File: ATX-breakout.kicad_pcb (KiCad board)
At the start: 2 copper layers, 67 x 59.5 mm, 21 parts, among them J1 I2C, J10 3V3 out, J11 12V out, J2 EPS, J3 USB_A, J4 Raspberry_Pi_2_3, J5 ATX24pin, J6 12V out, J7 pson ext, J8 5V out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

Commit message: Added readme
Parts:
- added G***: LOGO, graphics:kiwi, B.Cu at (114.6, 61.4)
- added G***: LOGO, graphics:kiwi, F.Cu at (69.0, 87.2)
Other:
- board text added: "PowerSelect"
- board text added: "git.io/PiATX"
- board text removed: "USB PowerSelect"

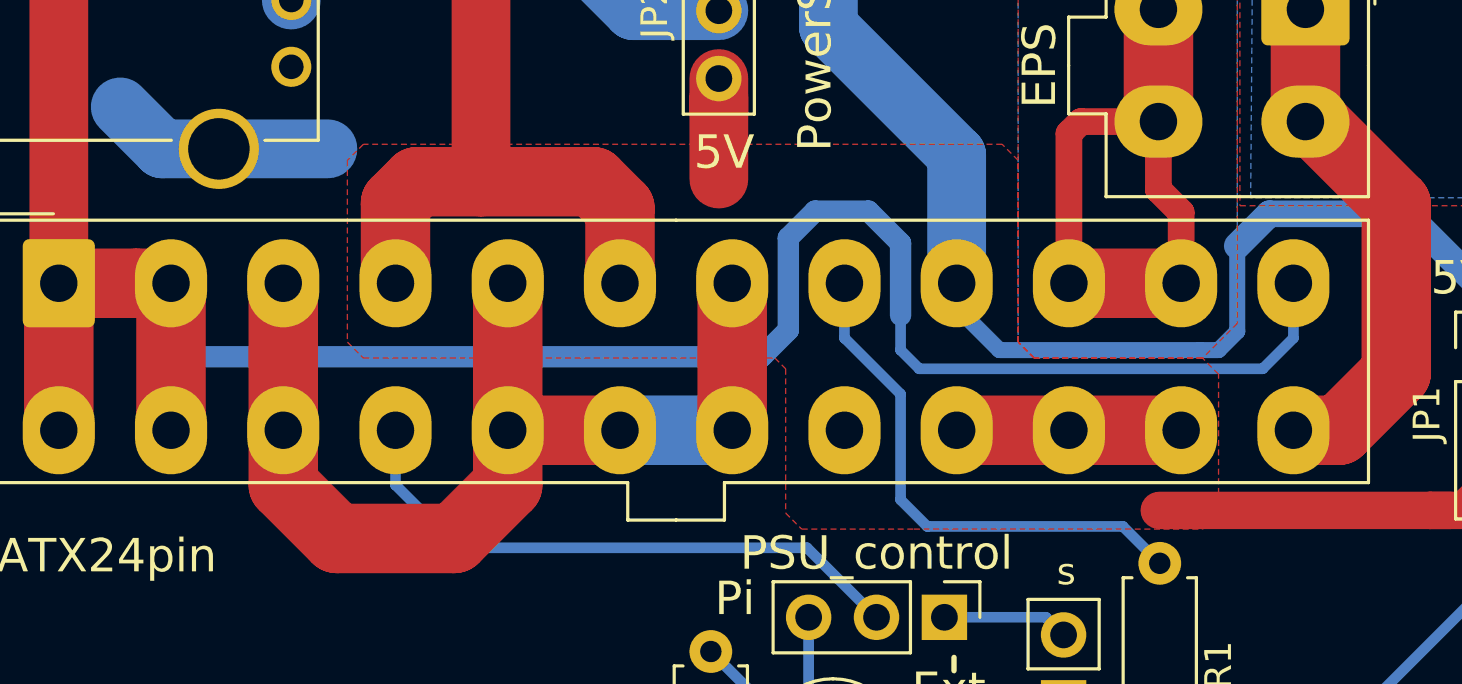
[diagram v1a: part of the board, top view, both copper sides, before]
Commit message: Made 12v pour solid, and increased 5v trace thicknesses
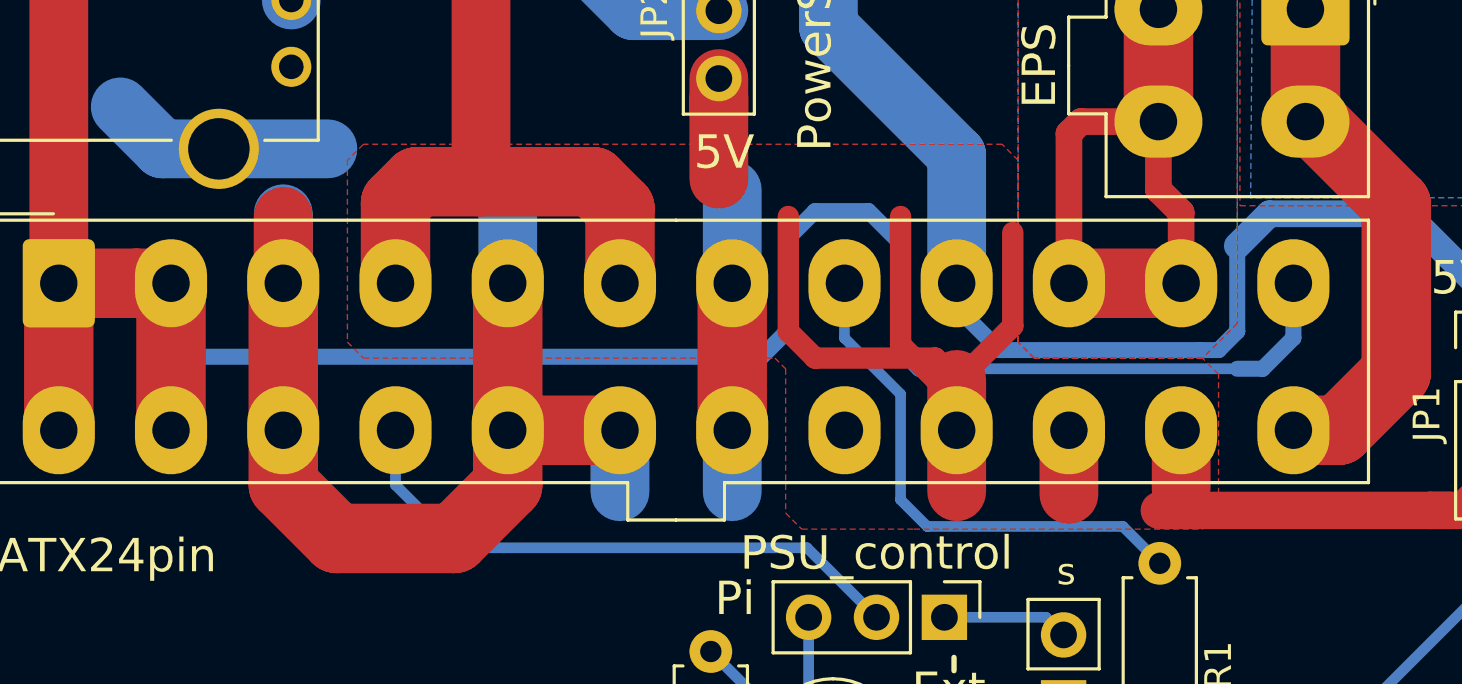
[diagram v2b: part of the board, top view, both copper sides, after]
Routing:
- net +5V: track 61.0 -> 86.6 mm
- net GND: track 107.2 -> 121.7 mm
- net +3V3: track 95.8 -> 96.6 mm

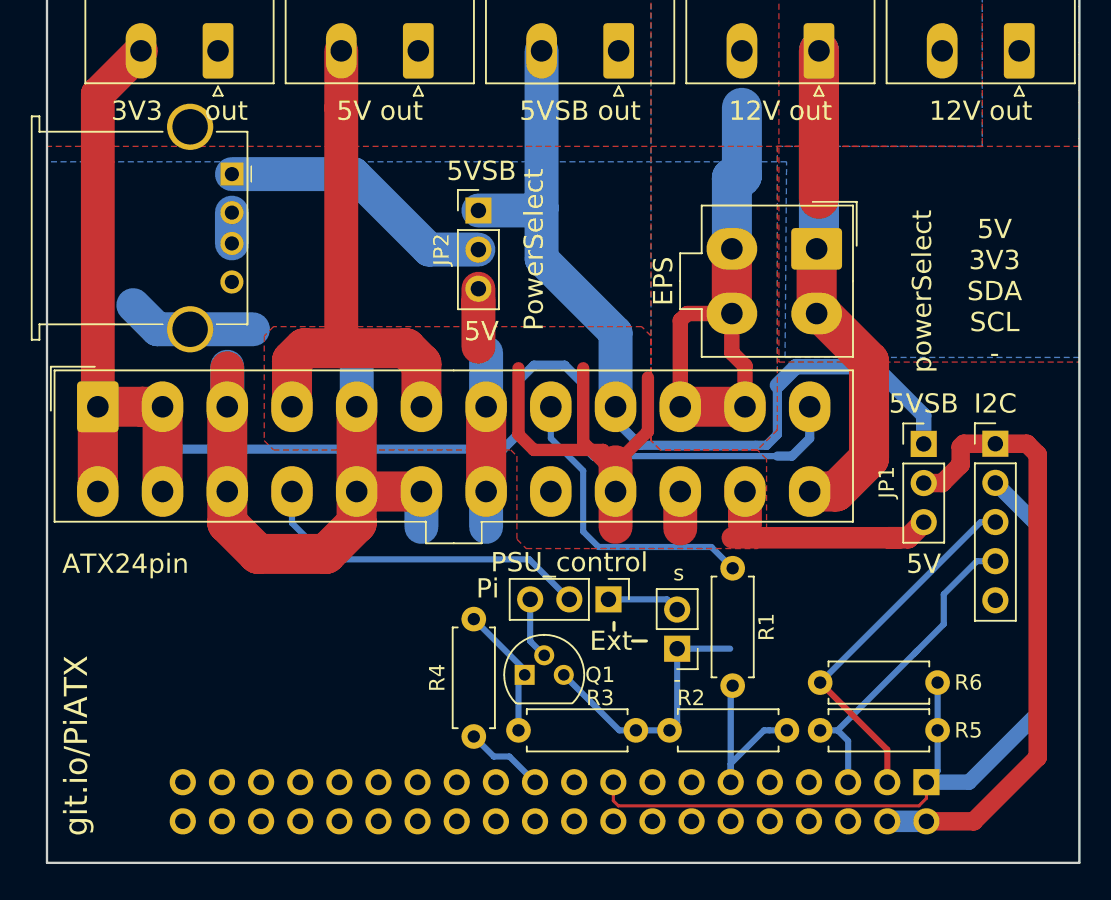
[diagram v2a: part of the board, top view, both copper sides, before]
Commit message: Fixed 3.3v shorted across lots of pins
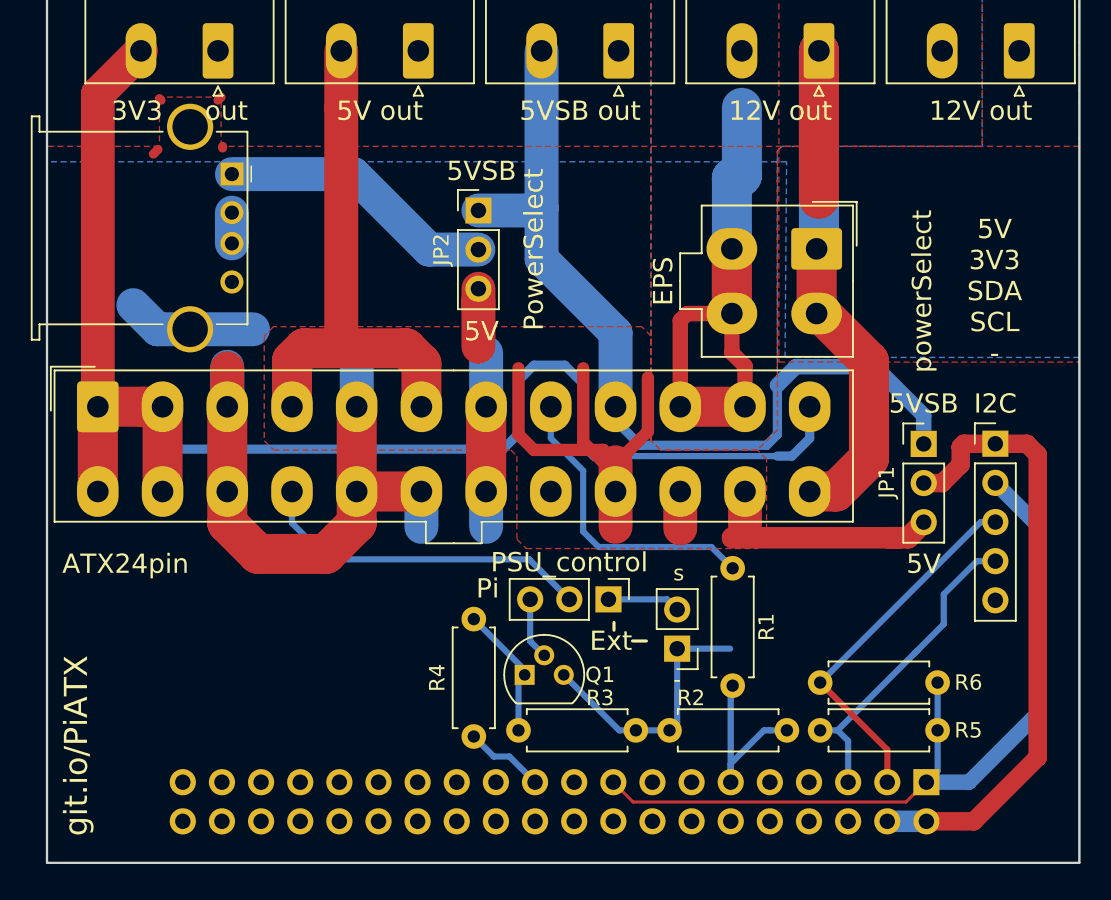
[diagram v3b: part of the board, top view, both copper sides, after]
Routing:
- net /3v3_rpi: track 54.8 -> 53.3 mm
- net (no net): track 0.00 -> 0.95 mm

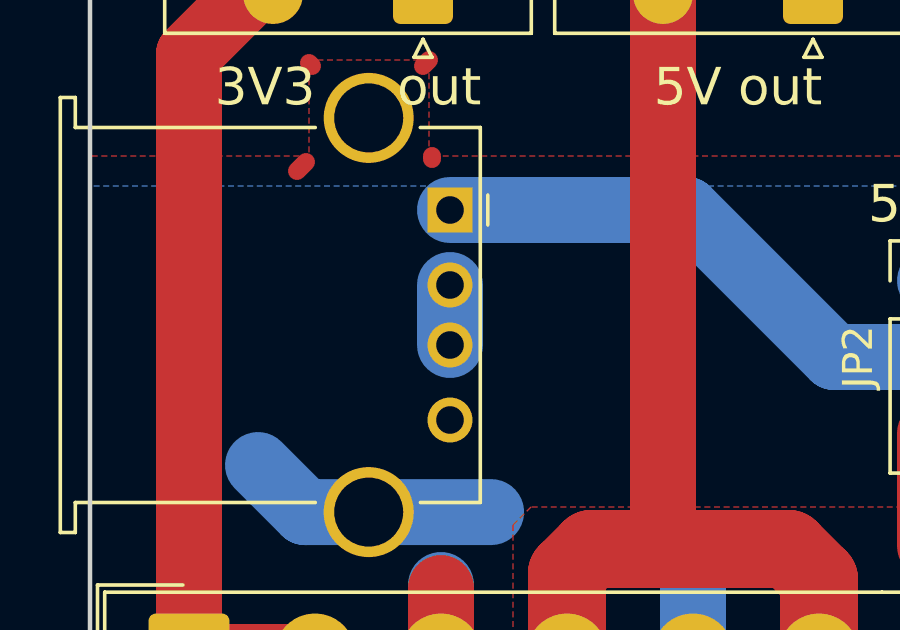
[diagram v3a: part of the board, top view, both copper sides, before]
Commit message: fixed ground-pour weirdness
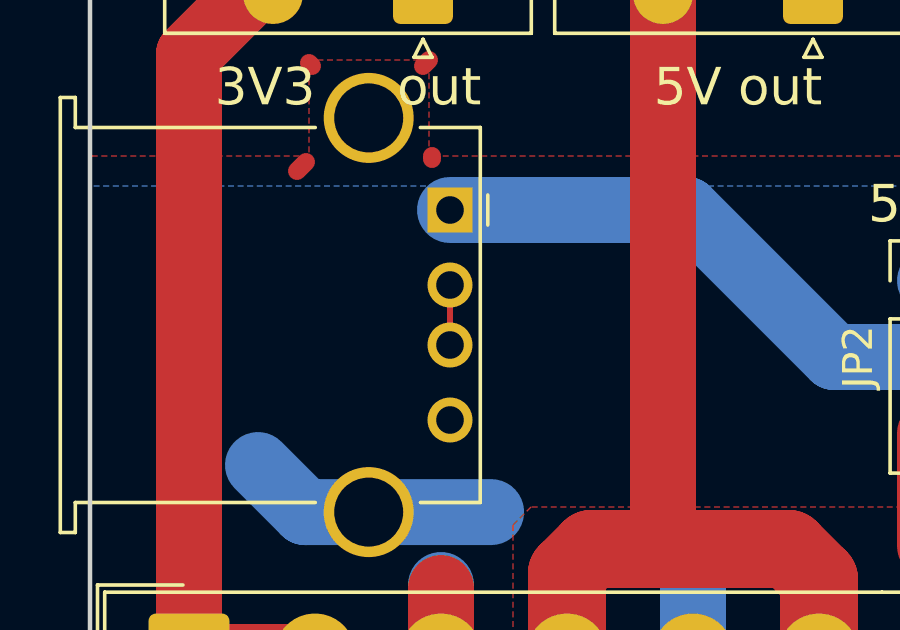
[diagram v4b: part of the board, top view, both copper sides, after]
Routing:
- net (no net): track 0.95 -> 0.00 mm
- net GND: track 121.7 -> 122.7 mm
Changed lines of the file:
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@@
   (gr_line (start 122 100) (end 122 40.5) (layer Edge.Cuts) (width 0.15))
   (gr_line (start 55 100) (end 122 100) (layer Edge.Cuts) (width 0.15))
-  (segment (start 62.4 50.5) (end 62.3 50.4) (width 0.6) (layer F.Cu) (net 0))
-  (segment (start 66.1 50.5) (end 66.3 50.3) (width 0.6) (layer F.Cu) (net 0))
-  (segment (start 66.4 53.5) (end 66.4 53.6) (width 0.6) (layer F.Cu) (net 0))
-  (segment (start 61.9 54) (end 62.2 53.7) (width 0.6) (layer F.Cu) (net 0))
+  (segment (start 62.4 50.5) (end 62.3 50.4) (width 0.6) (layer F.Cu) (net 3))
+  (segment (start 66.1 50.5) (end 66.3 50.3) (width 0.6) (layer F.Cu) (net 3))
+  (segment (start 66.4 53.5) (end 66.4 53.6) (width 0.6) (layer F.Cu) (net 3))
+  (segment (start 61.9 54) (end 62.2 53.7) (width 0.6) (layer F.Cu) (net 3))
   (segment (start 109.534999 97.305001) (end 112.074999 97.305001) (width 1.4) (layer B.Cu) (net 1))
   (segment (start 118.6 72.8) (end 116.55 72.8) (width 1.2) (layer F.Cu) (net 1))
@@
   (segment (start 74.9 55.3) (end 67 55.3) (width 2.2) (layer B.Cu) (net 15))
   (segment (start 79.8 60.2) (end 74.9 55.3) (width 2.2) (layer B.Cu) (net 15))
-  (segment (start 67 59.8) (end 67 57.8) (width 2.2) (layer B.Cu) (net 16))
+  (segment (start 67 57.8) (end 67 59.8) (width 0.2) (layer F.Cu) (net 16))
   (segment (start 109.534999 92.654999) (end 105.18 88.3) (width 0.4) (layer F.Cu) (net 17))
   (segment (start 109.534999 94.765001) (end 109.534999 92.654999) (width 0.4) (layer F.Cu) (net 17))

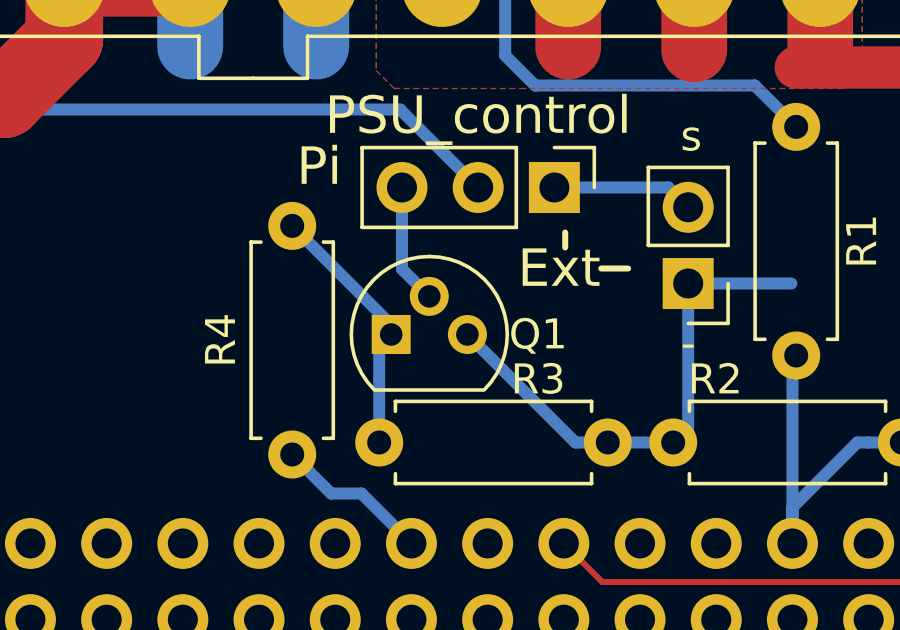
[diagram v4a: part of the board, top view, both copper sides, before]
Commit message: Switched to a more common transistor pinout
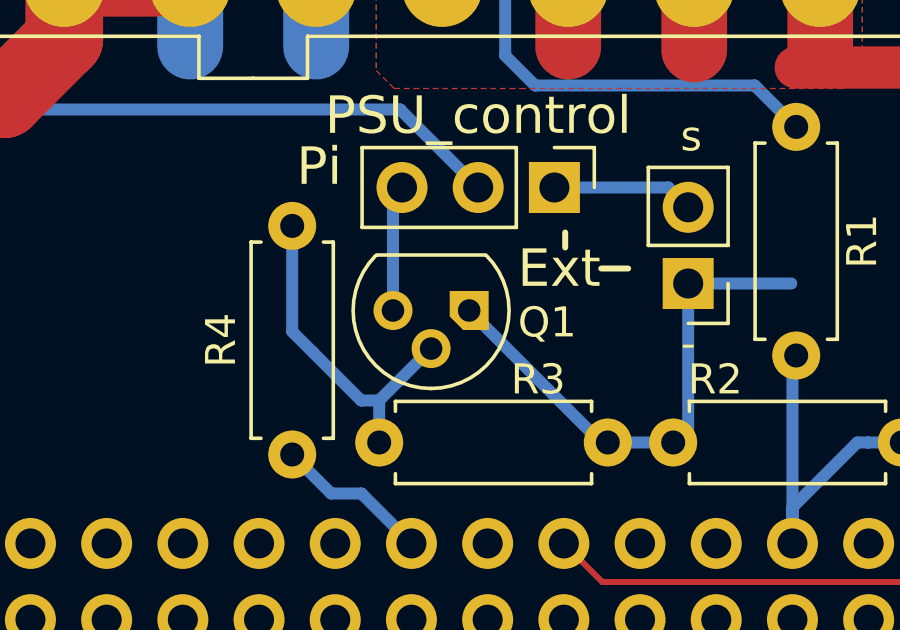
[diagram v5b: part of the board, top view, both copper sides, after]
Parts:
- moved Q1 2.72 mm to (88.6, 87.0), turned to 180 degrees
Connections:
- Q1 pad 1: Net-(Q1-Pad1) -> GND
- Q1 pad 2: Net-(JP3-Pad3) -> Net-(Q1-Pad2)
- Q1 pad 3: GND -> Net-(JP3-Pad3)
- R3 pad 1: Net-(Q1-Pad1) -> Net-(Q1-Pad2)
- R4 pad 2: Net-(Q1-Pad1) -> Net-(Q1-Pad2)
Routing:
- net Net-(Q1-Pad2): track 0.00 -> 11.2 mm
- net Net-(Q1-Pad1): track 8.75 -> 0.00 mm

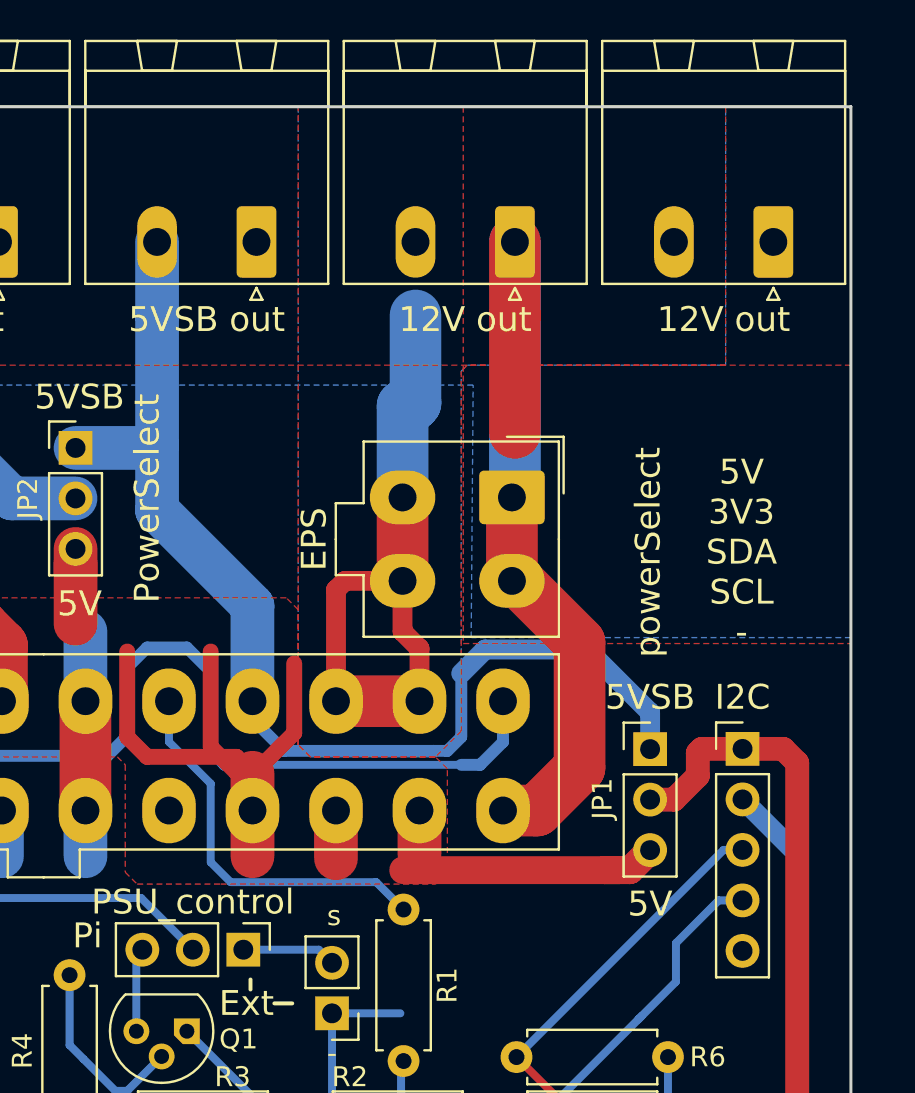
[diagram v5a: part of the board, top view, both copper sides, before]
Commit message: Added third 12v connector, fixed 12v-5v short
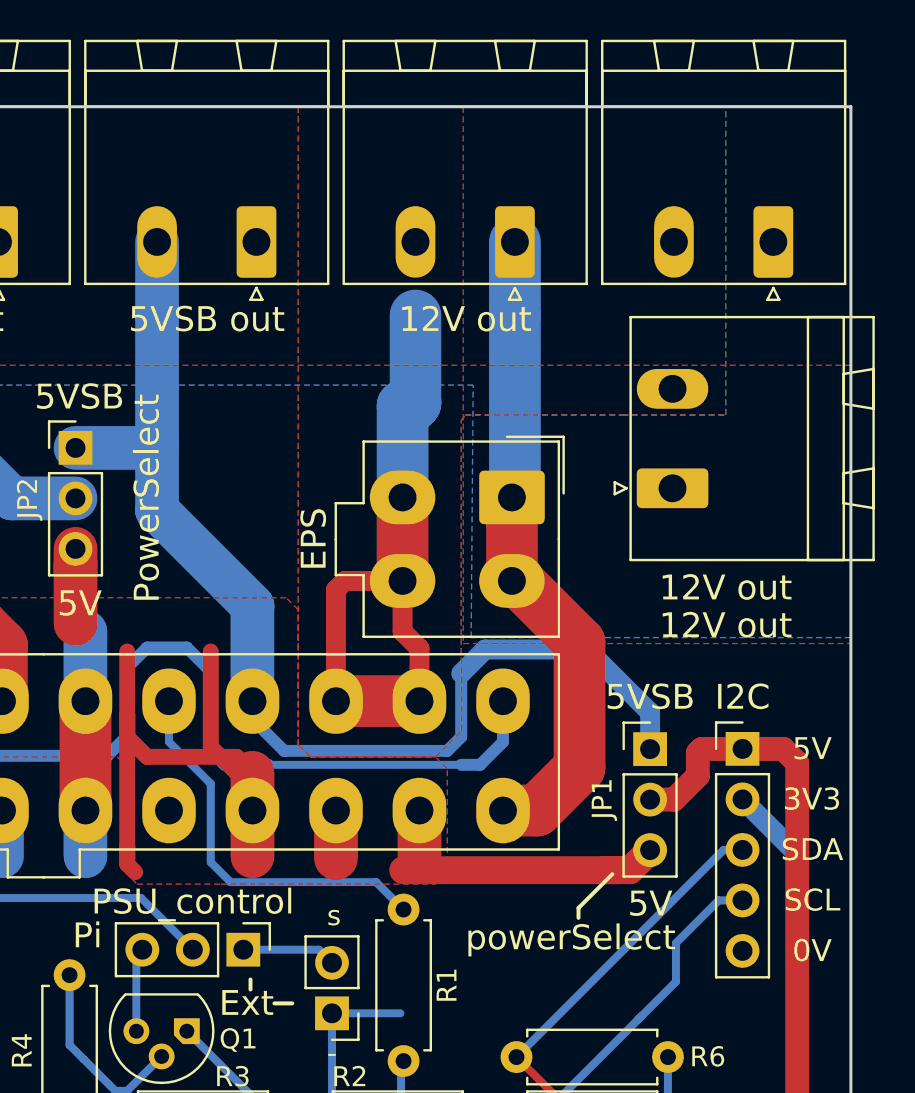
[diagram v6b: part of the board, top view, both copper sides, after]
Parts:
- added J12: 12V out, Connector_Phoenix_MSTB:PhoenixContact_MSTBA_2,5_2-G_1x02_P5.00mm_Horizontal, F.Cu at (113.0, 59.7)
- moved G*** 52.4 mm to (69.0, 87.2)
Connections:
- J4 pad 10: (no net) -> Net-(J4-Pad10)
- J4 pad 12: (no net) -> Net-(J4-Pad12)
- J4 pad 13: (no net) -> Net-(J4-Pad13)
- J4 pad 15: (no net) -> Net-(J4-Pad15)
- J4 pad 16: (no net) -> Net-(J4-Pad16)
- J4 pad 18: (no net) -> Net-(J4-Pad18)
- J4 pad 19: (no net) -> Net-(J4-Pad19)
- J4 pad 22: (no net) -> Net-(J4-Pad22)
- J4 pad 23: (no net) -> Net-(J4-Pad23)
- J4 pad 24: (no net) -> Net-(J4-Pad24)
- J4 pad 26: (no net) -> Net-(J4-Pad26)
- J4 pad 27: (no net) -> Net-(J4-Pad27)
- J4 pad 28: (no net) -> Net-(J4-Pad28)
- J4 pad 29: (no net) -> Net-(J4-Pad29)
- J4 pad 31: (no net) -> Net-(J4-Pad31)
- J4 pad 32: (no net) -> Net-(J4-Pad32)
- J4 pad 33: (no net) -> Net-(J4-Pad33)
- J4 pad 35: (no net) -> Net-(J4-Pad35)
- J4 pad 36: (no net) -> Net-(J4-Pad36)
- J4 pad 37: (no net) -> Net-(J4-Pad37)
- J4 pad 38: (no net) -> Net-(J4-Pad38)
- J4 pad 40: (no net) -> Net-(J4-Pad40)
- J4 pad 7: (no net) -> Net-(J4-Pad7)
- J4 pad 8: (no net) -> Net-(J4-Pad8)
- J5 pad 20: (no net) -> Net-(J5-Pad20)
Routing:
- net GND: track 122.9 -> 113.3 mm
- net +5V: track 86.6 -> 89.0 mm
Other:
- board text added: "0V"
- board text added: "3V3"
- board text added: "SCL"
- board text added: "SDA"
- board text removed: "5V 3V3 SDA SCL -"
